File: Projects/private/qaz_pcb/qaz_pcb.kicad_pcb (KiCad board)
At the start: 2 copper layers, 200 x 97.6 mm, 77 parts, among them U1 Frood

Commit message: update
- removed folders and files created with newer versions of KiCAD
- added frood-specific files
- made all the necessary changes in both schematics and pcb editor (footprints)
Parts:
- U1: footprint footprints:Frood_PinHeader_2x13+5_P2.54mm_Labels_Top -> ScottoKeebs_MCU:Frood_PinHeader_2x13+5_P2.54mm_Labels_Top

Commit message: Finalised qaz pcb
- finished the traces and connections
- merged all necessary symbols, footprints, and 3d models into the ScottoKicad files and folders
- added rotary encoder for the qaz (with schematic and 3d model)
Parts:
- added ENC_SW1: Rotary_Encoder_Switch, ScottoKeebs_Components:Rotary_Encoder_PEC11R-4220K-S0024, F.Cu at (208.2, 47.7)
- moved D24 16.0 mm to (130.0, 119.2)
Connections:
- U1 pad 23: unconnected-(U1-GPIO26-Pad23) -> Row 4
- U1 pad 24: unconnected-(U1-GPIO27-Pad24) -> Pin A
- U1 pad 25: unconnected-(U1-GPIO28-Pad25) -> Pin B
- U1 pad 29: unconnected-(U1-GND-Pad29) -> GND
- U1 pad 4: unconnected-(U1-GND-Pad4) -> GND
- U1 pad 5: unconnected-(U1-GND-Pad5) -> GND
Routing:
- net Row 3: track 0.00 -> 335.4 mm, vias 0 -> 1
- net Row 2: track 0.00 -> 301.5 mm, vias 0 -> 1
- net Row 1: track 0.00 -> 261.0 mm, vias 0 -> 1
- net Row 0: track 0.00 -> 224.0 mm, vias 0 -> 1
- net Column 9: track 0.00 -> 167.5 mm, vias 0 -> 6
- net Column 0: track 0.00 -> 137.4 mm, vias 0 -> 6
- net Column 8: track 0.00 -> 132.7 mm, vias 0 -> 6
- net Column 1: track 0.00 -> 120.8 mm, vias 0 -> 6
- net Column 7: track 0.00 -> 116.4 mm, vias 0 -> 6
- net Column 2: track 0.00 -> 111.4 mm, vias 0 -> 6
- net GND: track 0.00 -> 110.6 mm
- net Column 6: track 0.00 -> 95.8 mm, vias 0 -> 6
- net Row 4: track 0.00 -> 91.7 mm
- net Pin B: track 0.00 -> 82.3 mm
- net Column 4: track 0.00 -> 81.2 mm, vias 0 -> 6
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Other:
- outline, holes or cut-outs redrawn

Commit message: update
- renamed everything from ScottoKeebs to Kunsteak
- only updated the footprints and symbols relevant to the qaz project (all the other ones will have to be updated once they are used)
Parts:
- removed the REF** at (111.0, 126.4)
- removed the REF** at (151.4, 126.4)
- added REF**: Stabilizer_MX_2.00u, Kunsteak_Stabilizer:Stabilizer_MX_2.00u, F.Cu at (151.4, 126.4)
- added REF**: Stabilizer_MX_2.00u, Kunsteak_Stabilizer:Stabilizer_MX_2.00u, F.Cu at (111.0, 126.4)
- D1, D10, D11, D12, D13, D14, D15, D16, D17, D18, D19, D2, D20, D21, D22, D23, D24, D25, D26, D27, D28, D29, D3, D30, D31, D32, D33, D34, D35, D36, D37, D4, D5, D6, D7, D8, D9: footprint ScottoKeebs_Components:Diode_SOD-123 -> Kunsteak_Components:Diode_SOD-123
- ENC_SW1: footprint ScottoKeebs_Components:Rotary_Encoder_PEC11R-4220K-S0024 -> Kunsteak_Components:Rotary_Encoder_PEC11R-4220K-S0024
- S1, S12, S13, S14, S15, S16, S17, S18, S19, S2, S20, S22, S23, S24, S25, S26, S27, S28, S3, S30, S31, S32, S35, S36, S37, S4, S5, S6, S7, S8, S9: footprint ScottoKeebs_Hotswap:Hotswap_MX_1.00u -> Kunsteak_Hotswap:Hotswap_MX_1.00u
- S10, S11: footprint ScottoKeebs_Hotswap:Hotswap_MX_1.25u -> Kunsteak_Hotswap:Hotswap_MX_1.25u
- S21: footprint ScottoKeebs_Hotswap:Hotswap_MX_1.75u -> Kunsteak_Hotswap:Hotswap_MX_1.75u
- S29: footprint ScottoKeebs_Hotswap:Hotswap_MX_1.50u -> Kunsteak_Hotswap:Hotswap_MX_1.00u
- S33: footprint ScottoKeebs_Hotswap:Hotswap_MX_2.25u -> Kunsteak_Hotswap:Hotswap_MX_2.25u
- S34: footprint ScottoKeebs_Hotswap:Hotswap_MX_2.00u -> Kunsteak_Hotswap:Hotswap_MX_2.00u
- U1: footprint ScottoKeebs_MCU:Frood_PinHeader_2x13+5_P2.54mm_Labels_Top -> Kunsteak_MCU:Frood_PinHeader_2x13+5_P2.54mm_Labels_Top

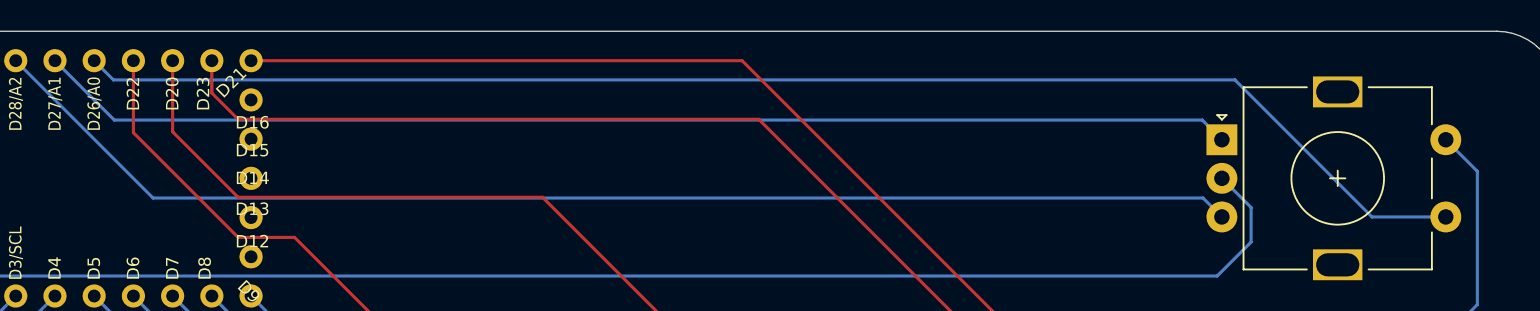
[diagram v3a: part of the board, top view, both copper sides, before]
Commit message: update
- fixed missing diode for rotary encoder
TODO:
- add mounting holes
- create case
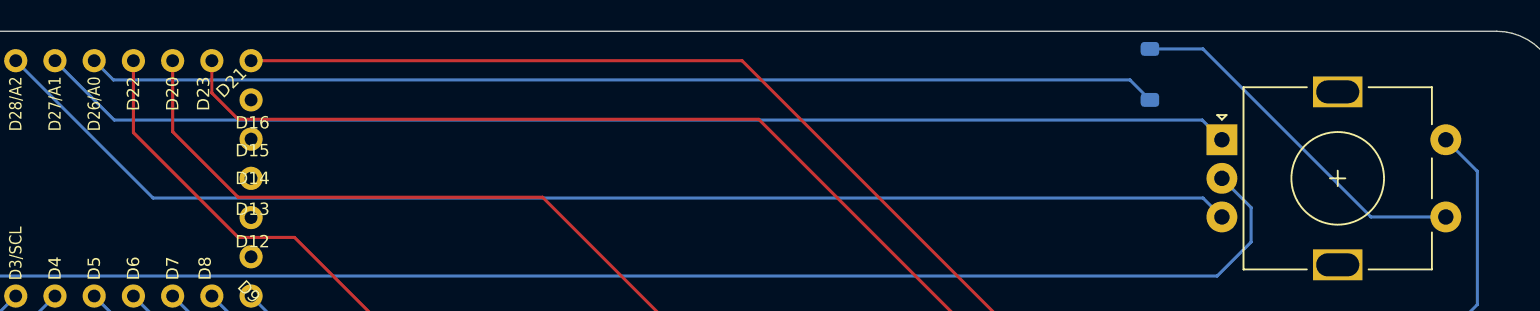
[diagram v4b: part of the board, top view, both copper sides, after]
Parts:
- added D38: Diode, Kunsteak_Components:Diode_SOD-123, B.Cu at (203.6, 43.4)
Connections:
- ENC_SW1 pad S1: Row 4 -> Net-(D38-A)
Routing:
- net Net-(D38-A): track 0.00 -> 23.7 mm
- net Row 4: track 91.7 -> 69.4 mm
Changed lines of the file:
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@@
   (net 65 "Pin A")
   (net 66 "Row 4")
+  (net 67 "Net-(D38-A)")
   (footprint "Kunsteak_Hotswap:Hotswap_MX_1.00u" (layer "F.Cu")
     (at 170.4975 107.315)
@@
     (pad "MP" thru_hole rect (at 7.5 8.1) (size 3.2 2) (drill oval 2.8 1.5) (layers "*.Cu" "*.Mask"))
     (pad "S1" thru_hole circle (at 14.5 5) (size 2 2) (drill 1) (layers "*.Cu" "*.Mask")
-      (net 66 "Row 4") (pinfunction "S1") (pintype "passive"))
+      (net 67 "Net-(D38-A)") (pinfunction "S1") (pintype "passive"))
     (pad "S2" thru_hole circle (at 14.5 0) (size 2 2) (drill 1) (layers "*.Cu" "*.Mask")
       (net 52 "Column 9") (pinfunction "S2") (pintype "passive"))
@@
   )
   (footprint "Kunsteak_Components:Diode_SOD-123" (layer "B.Cu")
+    (at 203.581 43.434 90)
+    (descr "SOD-123")
+    (tags "SOD-123")
+    (property "Sheetfile" "qaz_pcb.kicad_sch")
+    (property "Sheetname" "")
+    (property "Sim.Device" "D")
+    (property "Sim.Pins" "1=K 2=A")
+    (property "ki_description" "1N4148 (DO-35) or 1N4148W (SOD-123)")
+    (property "ki_keywords" "diode")
+    (attr smd)
+    (fp_text reference "D38" (at 0 2 90) (layer "B.SilkS")
+        (effects (font (size 1 1) (thickness 0.15)) (justify mirror))
+    )
+    (fp_text value "Diode" (at 0 -2.1 90) (layer "B.Fab")
+        (effects (font (size 1 1) (thickness 0.15)) (justify mirror))
+    )
+    (fp_text user "${REFERENCE}" (at 0 2 90) (layer "B.Fab")
+        (effects (font (size 1 1) (thickness 0.15)) (justify mirror))
+    )
+    (fp_line (start -0.75 0) (end -0.35 0)
+      (stroke (width 0.15) (type solid)) (layer "B.SilkS"))
+    (fp_line (start -0.35 0) (end -0.35 -0.55)
+      (stroke (width 0.15) (type solid)) (layer "B.SilkS"))
+    (fp_line (start -0.35 0) (end -0.35 0.55)
+      (stroke (width 0.15) (type solid)) (layer "B.SilkS"))
+    (fp_line (start -0.35 0) (end 0.25 0.4)
+      (stroke (width 0.15) (type solid)) (layer "B.SilkS"))
+    (fp_line (start 0.25 -0.4) (end -0.35 0)
+      (stroke (width 0.15) (type solid)) (layer "B.SilkS"))
+    (fp_line (start 0.25 0) (end 0.75 0)
+      (stroke (width 0.15) (type solid)) (layer "B.SilkS"))
+    (fp_line (start 0.25 0.4) (end 0.25 -0.4)
+      (stroke (width 0.15) (type solid)) (layer "B.SilkS"))
+    (fp_line (start -2.35 1.15) (end -2.35 -1.15)
+      (stroke (width 0.05) (type solid)) (layer "B.CrtYd"))
+    (fp_line (start -2.35 1.15) (end 2.35 1.15)
+      (stroke (width 0.05) (type solid)) (layer "B.CrtYd"))
+    (fp_line (start 2.35 -1.15) (end -2.35 -1.15)
+      (stroke (width 0.05) (type solid)) (layer "B.CrtYd"))
+    (fp_line (start 2.35 1.15) (end 2.35 -1.15)
+      (stroke (width 0.05) (type solid)) (layer "B.CrtYd"))
+    (fp_line (start -1.4 -0.9) (end -1.4 0.9)
+      (stroke (width 0.1) (type solid)) (layer "B.Fab"))
+    (fp_line (start -1.4 0.9) (end 1.4 0.9)
+      (stroke (width 0.1) (type solid)) (layer "B.Fab"))
+    (fp_line (start -0.75 0) (end -0.35 0)
+      (stroke (width 0.1) (type solid)) (layer "B.Fab"))
+    (fp_line (start -0.35 0) (end -0.35 -0.55)
+      (stroke (width 0.1) (type solid)) (layer "B.Fab"))
+    (fp_line (start -0.35 0) (end -0.35 0.55)
+      (stroke (width 0.1) (type solid)) (layer "B.Fab"))
+    (fp_line (start -0.35 0) (end 0.25 0.4)
+      (stroke (width 0.1) (type solid)) (layer "B.Fab"))
+    (fp_line (start 0.25 -0.4) (end -0.35 0)
+      (stroke (width 0.1) (type solid)) (layer "B.Fab"))
+    (fp_line (start 0.25 0) (end 0.75 0)
+      (stroke (width 0.1) (type solid)) (layer "B.Fab"))
+    (fp_line (start 0.25 0.4) (end 0.25 -0.4)
+      (stroke (width 0.1) (type solid)) (layer "B.Fab"))
+    (fp_line (start 1.4 -0.9) (end -1.4 -0.9)
+      (stroke (width 0.1) (type solid)) (layer "B.Fab"))
+    (fp_line (start 1.4 0.9) (end 1.4 -0.9)
+      (stroke (width 0.1) (type solid)) (layer "B.Fab"))
+    (pad "1" smd roundrect (at -1.65 0 90) (size 0.9 1.2) (layers "B.Cu" "B.Paste" "B.Mask") (roundrect_rratio 0.25)
+      (net 66 "Row 4") (pinfunction "K") (pintype "passive"))
+    (pad "2" smd roundrect (at 1.65 0 90) (size 0.9 1.2) (layers "B.Cu" "B.Paste" "B.Mask") (roundrect_rratio 0.25)
+      (net 67 "Net-(D38-A)") (pinfunction "A") (pintype "passive"))
+    (model "${KUNSTEAK_KICAD}/3dmodels/Kunsteak_Components.3dshapes/Diode_SOD-123.step"
+      (offset (xyz 0 0 0))
+      (scale (xyz 1 1 1))
+      (rotate (xyz 0 0 0))
+    )
+  )
+  (footprint "Kunsteak_Components:Diode_SOD-123" (layer "B.Cu")
     (at 53.81625 95.40875 90)
     (descr "SOD-123")
@@
   (segment (start 206.96625 46.39) (end 136.5145 46.39) (width 0.2) (layer "B.Cu") (net 65))
   (segment (start 208.24125 47.665) (end 206.96625 46.39) (width 0.2) (layer "B.Cu") (net 65))
-  (segment (start 209.085 43.79) (end 136.4545 43.79) (width 0.2) (layer "B.Cu") (net 66))
-  (segment (start 217.96 52.665) (end 209.085 43.79) (width 0.2) (layer "B.Cu") (net 66))
-  (segment (start 222.74125 52.665) (end 217.96 52.665) (width 0.2) (layer "B.Cu") (net 66))
-  (segment (start 136.4545 43.79) (end 135.2095 42.545) (width 0.2) (layer "B.Cu") (net 66))
+  (segment (start 136.4545 43.79) (end 202.287 43.79) (width 0.2) (layer "B.Cu") (net 66))
+  (segment (start 202.287 43.79) (end 203.581 45.084) (width 0.2) (layer "B.Cu") (net 66))
+  (segment (start 135.2095 42.545) (end 136.4545 43.79) (width 0.2) (layer "B.Cu") (net 66))
+  (segment (start 203.581 41.784) (end 207.011 41.784) (width 0.2) (layer "B.Cu") (net 67))
+  (segment (start 217.892 52.665) (end 222.74125 52.665) (width 0.2) (layer "B.Cu") (net 67))
+  (segment (start 207.011 41.784) (end 217.892 52.665) (width 0.2) (layer "B.Cu") (net 67))
 )

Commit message: Major update
- renamed everything from 'scottokeebs' and 'kunsteak' to 'personal' for easier access and personalisation/individualisation.
- updated README to include sources used in QAZ project
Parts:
- D1, D10, D11, D12, D13, D14, D15, D16, D17, D18, D19, D2, D20, D21, D22, D23, D24, D25, D26, D27, D28, D29, D3, D30, D31, D32, D33, D34, D35, D36, D37, D38, D4, D5, D6, D7, D8, D9: footprint Kunsteak_Components:Diode_SOD-123 -> Personal_Components:Diode_SOD-123
- ENC_SW1: footprint Kunsteak_Components:Rotary_Encoder_PEC11R-4220K-S0024 -> Personal_Components:Rotary_Encoder_PEC11R-4220K-S0024
- REF** (x2): footprint Kunsteak_Stabilizer:Stabilizer_MX_2.00u -> Personal_Stabilizer:Stabilizer_MX_2.00u
- S1, S12, S13, S14, S15, S16, S17, S18, S19, S2, S20, S22, S23, S24, S25, S26, S27, S28, S29, S3, S30, S31, S32, S35, S36, S37, S4, S5, S6, S7, S8, S9: footprint Kunsteak_Hotswap:Hotswap_MX_1.00u -> Personal_Hotswap:Hotswap_MX_1.00u
- S10, S11: footprint Kunsteak_Hotswap:Hotswap_MX_1.25u -> Personal_Hotswap:Hotswap_MX_1.25u
- S21: footprint Kunsteak_Hotswap:Hotswap_MX_1.75u -> Personal_Hotswap:Hotswap_MX_1.75u
- S33: footprint Kunsteak_Hotswap:Hotswap_MX_2.25u -> Personal_Hotswap:Hotswap_MX_2.25u
- S34: footprint Kunsteak_Hotswap:Hotswap_MX_2.00u -> Personal_Hotswap:Hotswap_MX_2.00u
- U1: footprint Kunsteak_MCU:Frood_PinHeader_2x13+5_P2.54mm_Labels_Top -> Personal_MCU:Frood_PinHeader_2x13+5_P2.54mm_Labels_Top
